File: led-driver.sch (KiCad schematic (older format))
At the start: 26 parts

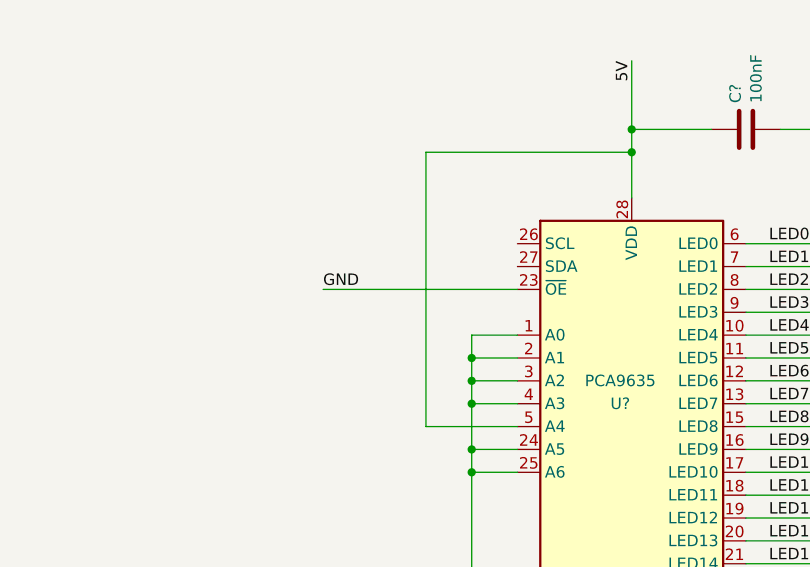
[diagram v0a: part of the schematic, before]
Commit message: added LED Driver sheet
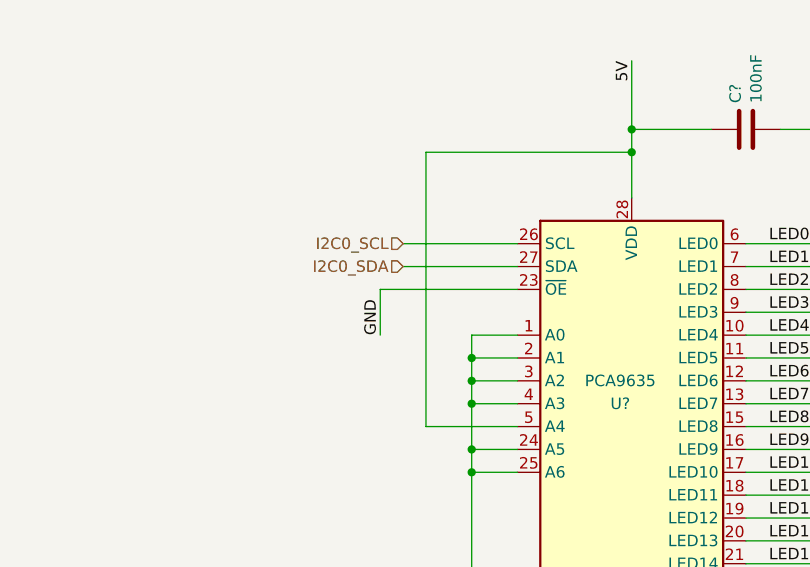
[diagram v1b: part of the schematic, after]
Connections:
- net I2C0_SCL: now reaches U?.26 (SCL)
- net I2C0_SDA: now reaches U?.27 (SDA)
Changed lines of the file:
@@
 AR Path="/5E2EDC4D/5E39412E" Ref="R?"  Part="1"
 AR Path="/5E3090FF/5E39412E" Ref="R?"  Part="1"
+AR Path="/5E30BD8E/5E39412E" Ref="R?"  Part="1"
 F 0 "R?" V 2650 5550 50  0000 L CNN
 F 1 "130" V 2670 5405 50  0000 L CNN
@@
 AR Path="/5E2EDC4D/5E394128" Ref="R?"  Part="1"
 AR Path="/5E3090FF/5E394128" Ref="R?"  Part="1"
+AR Path="/5E30BD8E/5E394128" Ref="R?"  Part="1"
 F 0 "R?" V 2650 5150 50  0000 L CNN
 F 1 "56" V 2670 5005 50  0000 L CNN
@@
 AR Path="/5E2EDC4D/5E394122" Ref="R?"  Part="1"
 AR Path="/5E3090FF/5E394122" Ref="R?"  Part="1"
+AR Path="/5E30BD8E/5E394122" Ref="R?"  Part="1"
 F 0 "R?" V 2650 5350 50  0000 L CNN
 F 1 "56" V 2670 5205 50  0000 L CNN
@@
 AR Path="/5E2EDC4D/5E37D737" Ref="R?"  Part="1"
 AR Path="/5E3090FF/5E37D737" Ref="R?"  Part="1"
+AR Path="/5E30BD8E/5E37D737" Ref="R?"  Part="1"
 F 0 "R?" V 4400 5550 50  0000 L CNN
 F 1 "130" V 4420 5405 50  0000 L CNN
@@
 AR Path="/5E2EDC4D/5E37D731" Ref="R?"  Part="1"
 AR Path="/5E3090FF/5E37D731" Ref="R?"  Part="1"
+AR Path="/5E30BD8E/5E37D731" Ref="R?"  Part="1"
 F 0 "R?" V 4400 5150 50  0000 L CNN
 F 1 "56" V 4420 5005 50  0000 L CNN
@@
 AR Path="/5E2EDC4D/5E37D72B" Ref="R?"  Part="1"
 AR Path="/5E3090FF/5E37D72B" Ref="R?"  Part="1"
+AR Path="/5E30BD8E/5E37D72B" Ref="R?"  Part="1"
 F 0 "R?" V 4400 5350 50  0000 L CNN
 F 1 "56" V 4420 5205 50  0000 L CNN
@@
 AR Path="/5E2EDC4D/5E3698FF" Ref="R?"  Part="1"
 AR Path="/5E3090FF/5E3698FF" Ref="R?"  Part="1"
+AR Path="/5E30BD8E/5E3698FF" Ref="R?"  Part="1"
 F 0 "R?" V 6150 5550 50  0000 L CNN
 F 1 "130" V 6170 5405 50  0000 L CNN
@@
 AR Path="/5E2EDC4D/5E3698F9" Ref="R?"  Part="1"
 AR Path="/5E3090FF/5E3698F9" Ref="R?"  Part="1"
+AR Path="/5E30BD8E/5E3698F9" Ref="R?"  Part="1"
 F 0 "R?" V 6150 5150 50  0000 L CNN
 F 1 "56" V 6170 5005 50  0000 L CNN
@@
 AR Path="/5E2EDC4D/5E3698F3" Ref="R?"  Part="1"
 AR Path="/5E3090FF/5E3698F3" Ref="R?"  Part="1"
+AR Path="/5E30BD8E/5E3698F3" Ref="R?"  Part="1"
 F 0 "R?" V 6150 5350 50  0000 L CNN
 F 1 "56" V 6170 5205 50  0000 L CNN
@@
 AR Path="/5E2EDC4D/5E32BEE6" Ref="R?"  Part="1"
 AR Path="/5E3090FF/5E32BEE6" Ref="R?"  Part="1"
+AR Path="/5E30BD8E/5E32BEE6" Ref="R?"  Part="1"
 F 0 "R?" V 7900 5550 50  0000 L CNN
 F 1 "130" V 7920 5405 50  0000 L CNN
@@
 AR Path="/5E2EDC4D/5E3273E4" Ref="R?"  Part="1"
 AR Path="/5E3090FF/5E3273E4" Ref="R?"  Part="1"
+AR Path="/5E30BD8E/5E3273E4" Ref="R?"  Part="1"
 F 0 "R?" V 7900 5150 50  0000 L CNN
 F 1 "56" V 7920 5005 50  0000 L CNN
@@
 AR Path="/5E2EDC4D/5E3286CA" Ref="R?"  Part="1"
 AR Path="/5E3090FF/5E3286CA" Ref="R?"  Part="1"
+AR Path="/5E30BD8E/5E3286CA" Ref="R?"  Part="1"
 F 0 "R?" V 7900 5350 50  0000 L CNN
 F 1 "56" V 7920 5205 50  0000 L CNN
@@
 AR Path="/5E2EDC4D/5E322DC6" Ref="C?"  Part="1"
 AR Path="/5E3090FF/5E322DC6" Ref="C?"  Part="1"
+AR Path="/5E30BD8E/5E322DC6" Ref="C?"  Part="1"
 F 0 "C?" H 8065 2146 50  0000 L CNN
 F 1 "100nF" H 8065 2055 50  0000 L CNN
@@
 Wire Wire Line
 	6550 3400 6950 3400
-Wire Wire Line
-	6100 2800 6950 2800
-Text Label 6100 2800 0    50   ~ 0
+Text Label 6350 3000 1    50   ~ 0
 GND
 Text Label 6950 4500 1    50   ~ 0
@@
 AR Path="/5E2EDC4D/5E41CE8E" Ref="C?"  Part="1"
 AR Path="/5E3090FF/5E41CE8E" Ref="C?"  Part="1"
+AR Path="/5E30BD8E/5E41CE8E" Ref="C?"  Part="1"
 F 0 "C?" H 2015 5896 50  0000 L CNN
 F 1 "10u" H 2015 5805 50  0000 L CNN
@@
 AR Path="/5E2EDC4D/5E423672" Ref="C?"  Part="1"
 AR Path="/5E3090FF/5E423672" Ref="C?"  Part="1"
+AR Path="/5E30BD8E/5E423672" Ref="C?"  Part="1"
 F 0 "C?" H 1565 5896 50  0000 L CNN
 F 1 "100nF" H 1565 5805 50  0000 L CNN
@@
 AR Path="/5E2EDC4D/5E43CDC8" Ref="C?"  Part="1"
 AR Path="/5E3090FF/5E43CDC8" Ref="C?"  Part="1"
+AR Path="/5E30BD8E/5E43CDC8" Ref="C?"  Part="1"
 F 0 "C?" H 3765 5896 50  0000 L CNN
 F 1 "10u" H 3765 5805 50  0000 L CNN
@@
 AR Path="/5E2EDC4D/5E43CDD1" Ref="C?"  Part="1"
 AR Path="/5E3090FF/5E43CDD1" Ref="C?"  Part="1"
+AR Path="/5E30BD8E/5E43CDD1" Ref="C?"  Part="1"
 F 0 "C?" H 3315 5896 50  0000 L CNN
 F 1 "100nF" H 3315 5805 50  0000 L CNN
@@
 AR Path="/5E2EDC4D/5E44029F" Ref="C?"  Part="1"
 AR Path="/5E3090FF/5E44029F" Ref="C?"  Part="1"
+AR Path="/5E30BD8E/5E44029F" Ref="C?"  Part="1"
 F 0 "C?" H 5515 5896 50  0000 L CNN
 F 1 "10u" H 5515 5805 50  0000 L CNN
@@
 AR Path="/5E2EDC4D/5E4402A8" Ref="C?"  Part="1"
 AR Path="/5E3090FF/5E4402A8" Ref="C?"  Part="1"
+AR Path="/5E30BD8E/5E4402A8" Ref="C?"  Part="1"
 F 0 "C?" H 5065 5896 50  0000 L CNN
 F 1 "100nF" H 5065 5805 50  0000 L CNN
@@
 AR Path="/5E2EDC4D/5E445DBC" Ref="C?"  Part="1"
 AR Path="/5E3090FF/5E445DBC" Ref="C?"  Part="1"
+AR Path="/5E30BD8E/5E445DBC" Ref="C?"  Part="1"
 F 0 "C?" H 7265 5896 50  0000 L CNN
 F 1 "10u" H 7265 5805 50  0000 L CNN
@@
 AR Path="/5E2EDC4D/5E445DC5" Ref="C?"  Part="1"
 AR Path="/5E3090FF/5E445DC5" Ref="C?"  Part="1"
+AR Path="/5E30BD8E/5E445DC5" Ref="C?"  Part="1"
 F 0 "C?" H 6815 5896 50  0000 L CNN
 F 1 "100nF" H 6815 5805 50  0000 L CNN
@@
 Wire Wire Line
 	7150 6100 7150 6350
+Text HLabel 6450 2700 0    50   Input ~ 0
+I2C0_SDA
+Wire Wire Line
+	6450 2700 6950 2700
+Text HLabel 6450 2600 0    50   Input ~ 0
+I2C0_SCL
+Wire Wire Line
+	6950 2600 6450 2600
+Wire Wire Line
+	6950 2800 6350 2800
+Wire Wire Line
+	6350 2800 6350 3000
 Wire Bus Line
 	3200 4650 3200 5350
